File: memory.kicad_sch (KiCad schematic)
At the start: 4 parts, among them U2 IS43TR16640C-125JBL

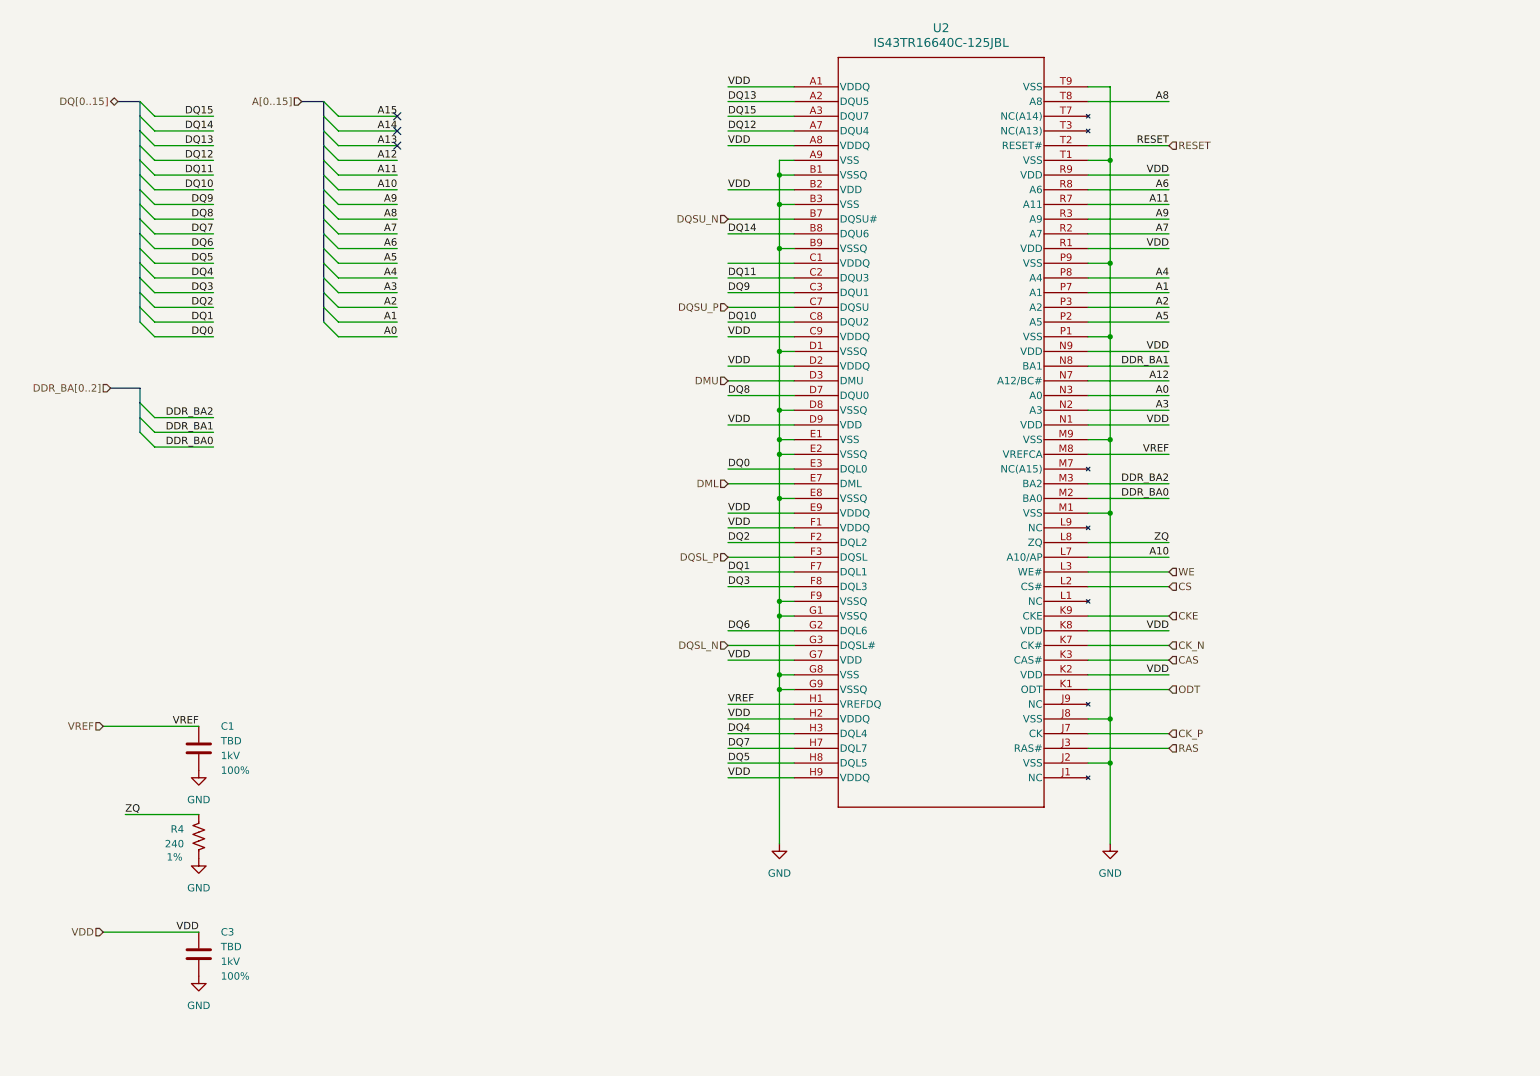
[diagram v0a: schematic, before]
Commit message: Added Power Nand USB
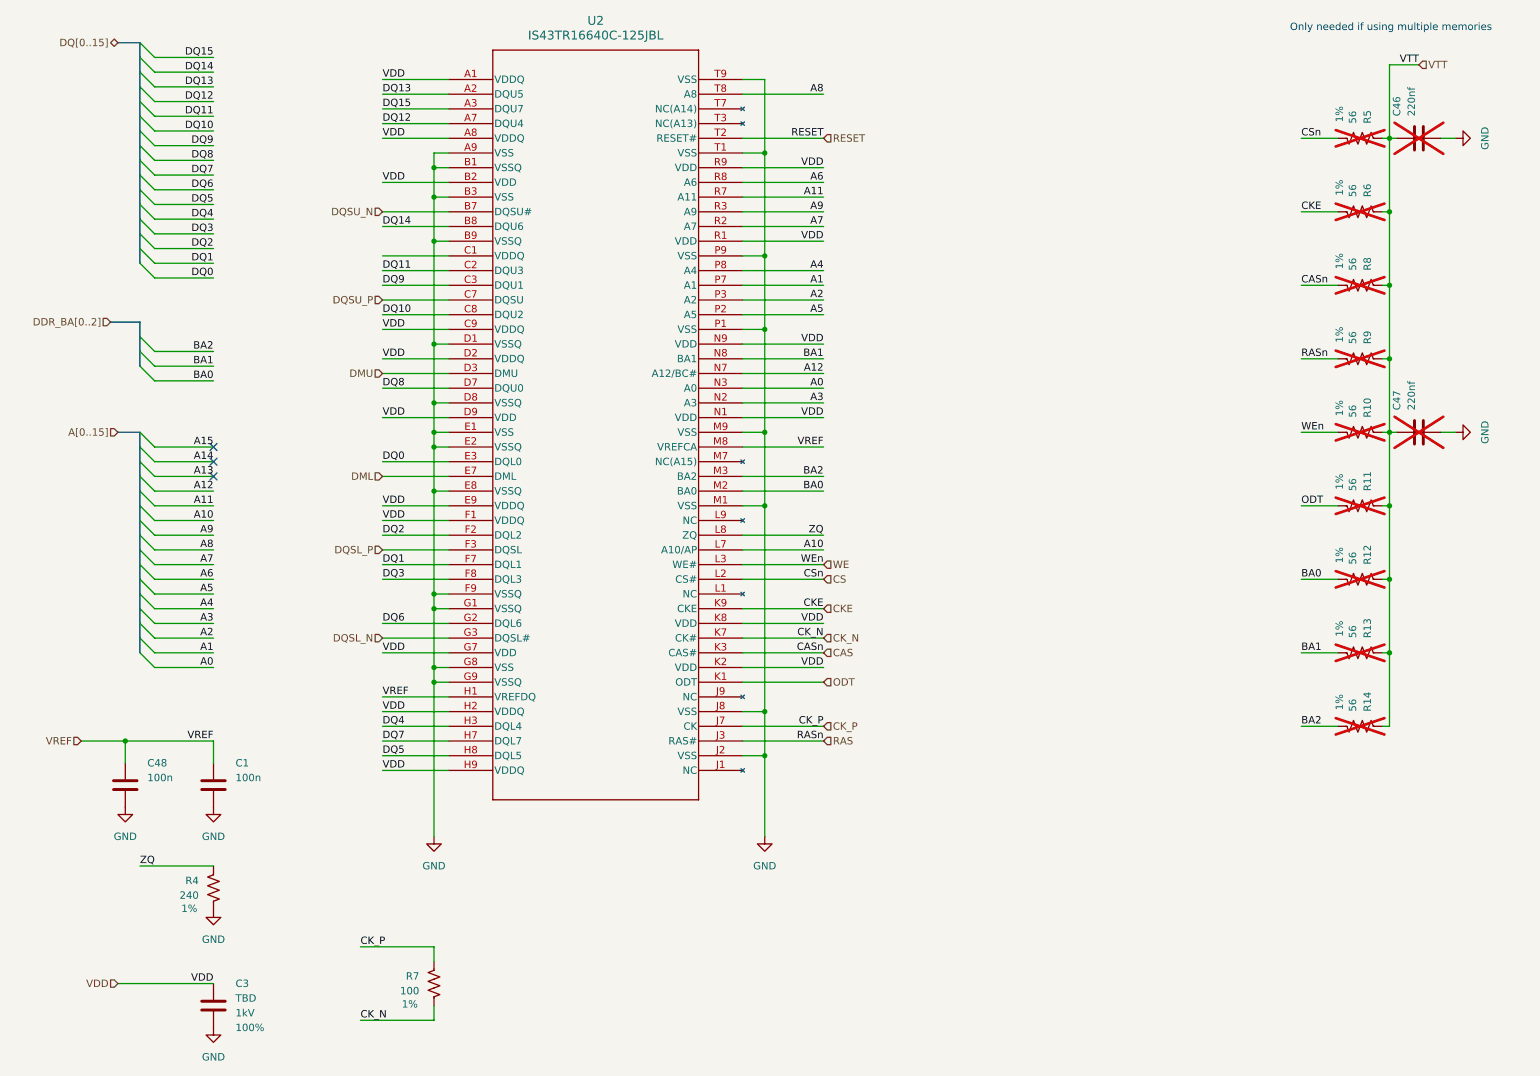
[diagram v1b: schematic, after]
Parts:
- added C46, C47: 220nf, TBD, symbol SparkFun-Capacitor:C
- added C48: 100n, symbol SparkFun-Capacitor:C
- added R10, R11, R12, R13, R14, R5, R6, R8, R9: 56, symbol SparkFun-Resistor:R
- added R7: 100, symbol SparkFun-Resistor:R
- C1: value TBD -> 100n; footprint TBD -> (none); Tolerance 100% -> (none); Voltage 1kV -> (none)
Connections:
- net CAS: now also R8.2
- net CKE: now also R6.2
- net CK_N: now also R7.2
- net CK_P: now also R7.1
- net CS: now also R5.2
- net GND: now also C46.2, C47.2, C48.2
- net ODT: now also R11.2
- net RAS: now also R9.2
- net VREF: now also C48.1
- net WE: now also R10.2
- net DDR_BA0 renamed BA0
- net BA0: now also R12.2
- net DDR_BA1 renamed BA1
- net BA1: now also R13.2
- net DDR_BA2 renamed BA2
- net BA2: now also R14.2
- new net VTT: C46.1, C47.1, R10.1, R11.1, R12.1, R13.1, R14.1, R5.1, R6.1, R8.1, R9.1
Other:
- note added: "Only needed if using multiple memories"
- moved on the sheet: C1, C3, R4, U2

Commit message: Adding more decoupling and started on DSI connector
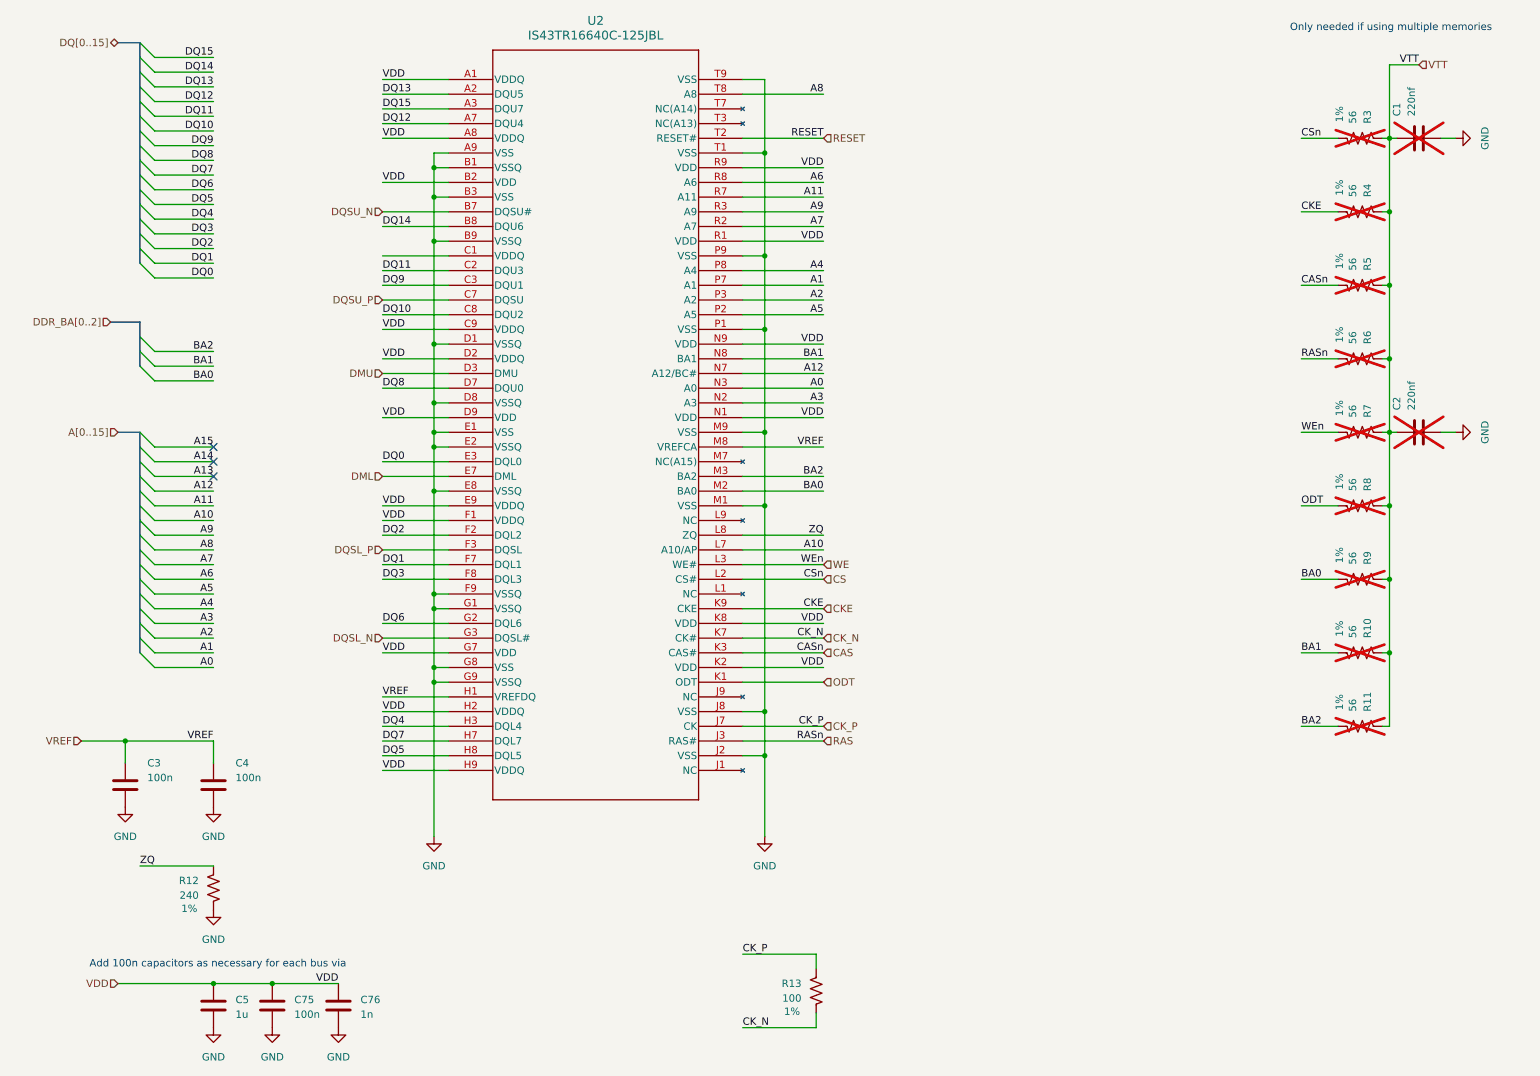
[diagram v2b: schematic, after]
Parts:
- added C75: 100n, symbol SparkFun-Capacitor:C
- added C76: 1n, symbol SparkFun-Capacitor:C
- C5: renamed from C3; value TBD -> 1u; footprint TBD -> (none); Tolerance 100% -> (none); Voltage 1kV -> (none)
- U2: footprint TW-BGA96L_9X13X1.2_ISI -> (none)
- renumbered C46 to C1, C47 to C2, C48 to C3, C1 to C4, R13 to R10, R14 to R11, R4 to R12, R7 to R13, R5 to R3, R6 to R4, R8 to R5, R9 to R6, R10 to R7, R11 to R8, R12 to R9
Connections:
- net GND: now also C75.2, C76.2
- net VDD: now also C75.1, C76.1
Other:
- note added: "Add 100n capacitors as necessary for each bus via"
- moved on the sheet: R13

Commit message: Selecting footprints
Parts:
- C3, C4, C5: footprint (none) -> Capacitor_SMD:C_0402_1005Metric
- C6: renamed from C75; footprint (none) -> Capacitor_SMD:C_0402_1005Metric
- C7: renamed from C76; footprint (none) -> Capacitor_SMD:C_0402_1005Metric
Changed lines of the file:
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@@
 			)
 		)
-		(property "Footprint" ""
+		(property "Footprint" "Capacitor_SMD:C_0402_1005Metric"
 			(at 36.5252 161.29 0)
 			(effects
@@
 			)
 		)
-		(property "Footprint" ""
+		(property "Footprint" "Capacitor_SMD:C_0402_1005Metric"
 			(at 51.7652 199.39 0)
 			(effects
@@
 		(on_board yes)
 		(dnp no)
-		(property "Reference" "C75"
+		(property "Reference" "C6"
 			(at 64.77 186.944 0)
 			(effects
@@
 			)
 		)
-		(property "Footprint" ""
+		(property "Footprint" "Capacitor_SMD:C_0402_1005Metric"
 			(at 61.9252 199.39 0)
 			(effects
@@
 			(project "SBC"
 				(path "/21bb932a-ec67-4661-9215-0551f718d1c0/1a39d522-2eb7-49c0-a4cb-6db909b7fe44"
-					(reference "C75")
+					(reference "C6")
 					(unit 1)
 				)
@@
 		(dnp no)
 		(fields_autoplaced yes)
-		(property "Reference" "#PWR0143"
+		(property "Reference" "#PWR049"
 			(at 72.39 198.12 0)
 			(effects
@@
 			(project "SBC"
 				(path "/21bb932a-ec67-4661-9215-0551f718d1c0/1a39d522-2eb7-49c0-a4cb-6db909b7fe44"
-					(reference "#PWR0143")
+					(reference "#PWR049")
 					(unit 1)
 				)
@@
 		(dnp no)
 		(fields_autoplaced yes)
-		(property "Reference" "#PWR0142"
+		(property "Reference" "#PWR048"
 			(at 60.96 198.12 0)
 			(effects
@@
 			(project "SBC"
 				(path "/21bb932a-ec67-4661-9215-0551f718d1c0/1a39d522-2eb7-49c0-a4cb-6db909b7fe44"
-					(reference "#PWR0142")
+					(reference "#PWR048")
 					(unit 1)
 				)
@@
 		(on_board yes)
 		(dnp no)
-		(property "Reference" "C76"
+		(property "Reference" "C7"
 			(at 76.2 186.944 0)
 			(effects
@@
 			)
 		)
-		(property "Footprint" ""
+		(property "Footprint" "Capacitor_SMD:C_0402_1005Metric"
 			(at 73.3552 199.39 0)
 			(effects
@@
 			(project "SBC"
 				(path "/21bb932a-ec67-4661-9215-0551f718d1c0/1a39d522-2eb7-49c0-a4cb-6db909b7fe44"
-					(reference "C76")
+					(reference "C7")
 					(unit 1)
 				)
@@
 			)
 		)
-		(property "Footprint" ""
+		(property "Footprint" "Capacitor_SMD:C_0402_1005Metric"
 			(at 51.7652 161.29 0)
 			(effects

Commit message: Added all footprints and kicked off pcb design
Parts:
- R12, R13: footprint (none) -> Resistor_SMD:R_0402_1005Metric
- U2: footprint (none) -> footprints:TW-BGA96L_9X13X1.2_ISI
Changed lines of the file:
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@@
 			)
 		)
-		(property "Footprint" ""
+		(property "Footprint" "Resistor_SMD:R_0402_1005Metric"
 			(at 46.228 167.64 0)
 			(effects
@@
 			)
 		)
-		(property "Footprint" ""
+		(property "Footprint" "footprints:TW-BGA96L_9X13X1.2_ISI"
 			(at 91.44 27.94 0)
 			(effects
@@
 			)
 		)
-		(property "Footprint" ""
+		(property "Footprint" "Resistor_SMD:R_0402_1005Metric"
 			(at 150.368 185.42 0)
 			(effects

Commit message: Layout started
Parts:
- renumbered R3 to R17, R4 to R18, R5 to R19, R6 to R20, R7 to R21, R8 to R22, R9 to R23, R10 to R24, R11 to R25, R12 to R26, R13 to R27
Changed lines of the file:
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@@
 		(on_board no)
 		(dnp yes)
-		(property "Reference" "R9"
+		(property "Reference" "R23"
 			(at 250.1901 111.76 90)
 			(effects
@@
 			(project "SBC"
 				(path "/21bb932a-ec67-4661-9215-0551f718d1c0/1a39d522-2eb7-49c0-a4cb-6db909b7fe44"
-					(reference "R9")
+					(reference "R23")
 					(unit 1)
 				)
@@
 		(dnp no)
 		(fields_autoplaced yes)
-		(property "Reference" "#PWR041"
+		(property "Reference" "#PWR056"
 			(at 271.78 88.9 0)
 			(effects
@@
 			(project "SBC"
 				(path "/21bb932a-ec67-4661-9215-0551f718d1c0/1a39d522-2eb7-49c0-a4cb-6db909b7fe44"
-					(reference "#PWR041")
+					(reference "#PWR056")
 					(unit 1)
 				)
@@
 		(dnp no)
 		(fields_autoplaced yes)
-		(property "Reference" "#PWR049"
+		(property "Reference" "#PWR064"
 			(at 72.39 198.12 0)
 			(effects
@@
 			(project "SBC"
 				(path "/21bb932a-ec67-4661-9215-0551f718d1c0/1a39d522-2eb7-49c0-a4cb-6db909b7fe44"
-					(reference "#PWR049")
+					(reference "#PWR064")
 					(unit 1)
 				)
@@
 		(dnp no)
 		(fields_autoplaced yes)
-		(property "Reference" "#PWR048"
+		(property "Reference" "#PWR063"
 			(at 60.96 198.12 0)
 			(effects
@@
 			(project "SBC"
 				(path "/21bb932a-ec67-4661-9215-0551f718d1c0/1a39d522-2eb7-49c0-a4cb-6db909b7fe44"
-					(reference "#PWR048")
+					(reference "#PWR063")
 					(unit 1)
 				)
@@
 		(on_board no)
 		(dnp yes)
-		(property "Reference" "R5"
+		(property "Reference" "R19"
 			(at 250.1901 60.96 90)
 			(effects
@@
 			(project "SBC"
 				(path "/21bb932a-ec67-4661-9215-0551f718d1c0/1a39d522-2eb7-49c0-a4cb-6db909b7fe44"
-					(reference "R5")
+					(reference "R19")
 					(unit 1)
 				)
@@
 		(dnp no)
 		(fields_autoplaced yes)
-		(property "Reference" "#PWR045"
+		(property "Reference" "#PWR060"
 			(at 146.05 165.1 0)
 			(effects
@@
 			(project "SBC"
 				(path "/21bb932a-ec67-4661-9215-0551f718d1c0/1a39d522-2eb7-49c0-a4cb-6db909b7fe44"
-					(reference "#PWR045")
+					(reference "#PWR060")
 					(unit 1)
 				)
@@
 		(on_board no)
 		(dnp yes)
-		(property "Reference" "R7"
+		(property "Reference" "R21"
 			(at 250.1901 86.36 90)
 			(effects
@@
 			(project "SBC"
 				(path "/21bb932a-ec67-4661-9215-0551f718d1c0/1a39d522-2eb7-49c0-a4cb-6db909b7fe44"
-					(reference "R7")
+					(reference "R21")
 					(unit 1)
 				)
@@
 		(dnp no)
 		(fields_autoplaced yes)
-		(property "Reference" "#PWR040"
+		(property "Reference" "#PWR055"
 			(at 271.78 38.1 0)
 			(effects
@@
 			(project "SBC"
 				(path "/21bb932a-ec67-4661-9215-0551f718d1c0/1a39d522-2eb7-49c0-a4cb-6db909b7fe44"
-					(reference "#PWR040")
+					(reference "#PWR055")
 					(unit 1)
 				)
@@
 		(dnp no)
 		(fields_autoplaced yes)
-		(property "Reference" "#PWR043"
+		(property "Reference" "#PWR058"
 			(at 50.8 160.02 0)
 			(effects
@@
 			(project ""
 				(path "/21bb932a-ec67-4661-9215-0551f718d1c0/1a39d522-2eb7-49c0-a4cb-6db909b7fe44"
-					(reference "#PWR043")
+					(reference "#PWR058")
 					(unit 1)
 				)
@@
 		(on_board no)
 		(dnp yes)
-		(property "Reference" "R4"
+		(property "Reference" "R18"
 			(at 250.1901 48.26 90)
 			(effects
@@
 			(project "SBC"
 				(path "/21bb932a-ec67-4661-9215-0551f718d1c0/1a39d522-2eb7-49c0-a4cb-6db909b7fe44"
-					(reference "R4")
+					(reference "R18")
 					(unit 1)
 				)
@@
 		(on_board no)
 		(dnp yes)
-		(property "Reference" "R6"
+		(property "Reference" "R20"
 			(at 250.1901 73.66 90)
 			(effects
@@
 			(project "SBC"
 				(path "/21bb932a-ec67-4661-9215-0551f718d1c0/1a39d522-2eb7-49c0-a4cb-6db909b7fe44"
-					(reference "R6")
+					(reference "R20")
 					(unit 1)
 				)
@@
 		(on_board yes)
 		(dnp no)
-		(property "Reference" "R12"
+		(property "Reference" "R26"
 			(at 48.26 166.3699 90)
 			(effects
@@
 			(project "SBC"
 				(path "/21bb932a-ec67-4661-9215-0551f718d1c0/1a39d522-2eb7-49c0-a4cb-6db909b7fe44"
-					(reference "R12")
+					(reference "R26")
 					(unit 1)
 				)
@@
 		(dnp no)
 		(fields_autoplaced yes)
-		(property "Reference" "#PWR047"
+		(property "Reference" "#PWR062"
 			(at 50.8 198.12 0)
 			(effects
@@
 			(project "SBC"
 				(path "/21bb932a-ec67-4661-9215-0551f718d1c0/1a39d522-2eb7-49c0-a4cb-6db909b7fe44"
-					(reference "#PWR047")
+					(reference "#PWR062")
 					(unit 1)
 				)
@@
 		(on_board no)
 		(dnp yes)
-		(property "Reference" "R3"
+		(property "Reference" "R17"
 			(at 250.1901 35.56 90)
 			(effects
@@
 			(project "SBC"
 				(path "/21bb932a-ec67-4661-9215-0551f718d1c0/1a39d522-2eb7-49c0-a4cb-6db909b7fe44"
-					(reference "R3")
+					(reference "R17")
 					(unit 1)
 				)
@@
 		(on_board no)
 		(dnp yes)
-		(property "Reference" "R8"
+		(property "Reference" "R22"
 			(at 250.1901 99.06 90)
 			(effects
@@
 			(project "SBC"
 				(path "/21bb932a-ec67-4661-9215-0551f718d1c0/1a39d522-2eb7-49c0-a4cb-6db909b7fe44"
-					(reference "R8")
+					(reference "R22")
 					(unit 1)
 				)
@@
 		(on_board yes)
 		(dnp no)
-		(property "Reference" "R13"
+		(property "Reference" "R27"
 			(at 152.4 184.1499 90)
 			(effects
@@
 			(project "SBC"
 				(path "/21bb932a-ec67-4661-9215-0551f718d1c0/1a39d522-2eb7-49c0-a4cb-6db909b7fe44"
-					(reference "R13")
+					(reference "R27")
 					(unit 1)
 				)
@@
 		(dnp no)
 		(fields_autoplaced yes)
-		(property "Reference" "#PWR044"
+		(property "Reference" "#PWR059"
 			(at 88.9 165.1 0)
 			(effects
@@
 			(project "SBC"
 				(path "/21bb932a-ec67-4661-9215-0551f718d1c0/1a39d522-2eb7-49c0-a4cb-6db909b7fe44"
-					(reference "#PWR044")
+					(reference "#PWR059")
 					(unit 1)
 				)
@@
 		(dnp no)
 		(fields_autoplaced yes)
-		(property "Reference" "#PWR042"
+		(property "Reference" "#PWR057"
 			(at 35.56 160.02 0)
 			(effects
@@
 			(project "SBC"
 				(path "/21bb932a-ec67-4661-9215-0551f718d1c0/1a39d522-2eb7-49c0-a4cb-6db909b7fe44"
-					(reference "#PWR042")
+					(reference "#PWR057")
 					(unit 1)
 				)
@@
 		(dnp no)
 		(fields_autoplaced yes)
-		(property "Reference" "#PWR046"
+		(property "Reference" "#PWR061"
 			(at 50.8 177.8 0)
 			(effects
@@
 			(project "SBC"
 				(path "/21bb932a-ec67-4661-9215-0551f718d1c0/1a39d522-2eb7-49c0-a4cb-6db909b7fe44"
-					(reference "#PWR046")
+					(reference "#PWR061")
 					(unit 1)
 				)
@@
 		(on_board no)
 		(dnp yes)
-		(property "Reference" "R10"
+		(property "Reference" "R24"
 			(at 250.1901 124.46 90)
 			(effects
@@
 			(project "SBC"
 				(path "/21bb932a-ec67-4661-9215-0551f718d1c0/1a39d522-2eb7-49c0-a4cb-6db909b7fe44"
-					(reference "R10")
+					(reference "R24")
 					(unit 1)
 				)
@@
 		(on_board no)
 		(dnp yes)
-		(property "Reference" "R11"
+		(property "Reference" "R25"
 			(at 250.1901 137.16 90)
 			(effects
@@
 			(project "SBC"
 				(path "/21bb932a-ec67-4661-9215-0551f718d1c0/1a39d522-2eb7-49c0-a4cb-6db909b7fe44"
-					(reference "R11")
-					(unit 1)
-				)
+					(reference "R25")
+					(unit 1)
+				)
